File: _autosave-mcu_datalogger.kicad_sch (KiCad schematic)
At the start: 25 parts, among them U1 DS1337S_, U2 ATMEGA328P-AU, U3 24LC1025, U4 24LC1025, Y1 32.768MHz, Y2 16MHz

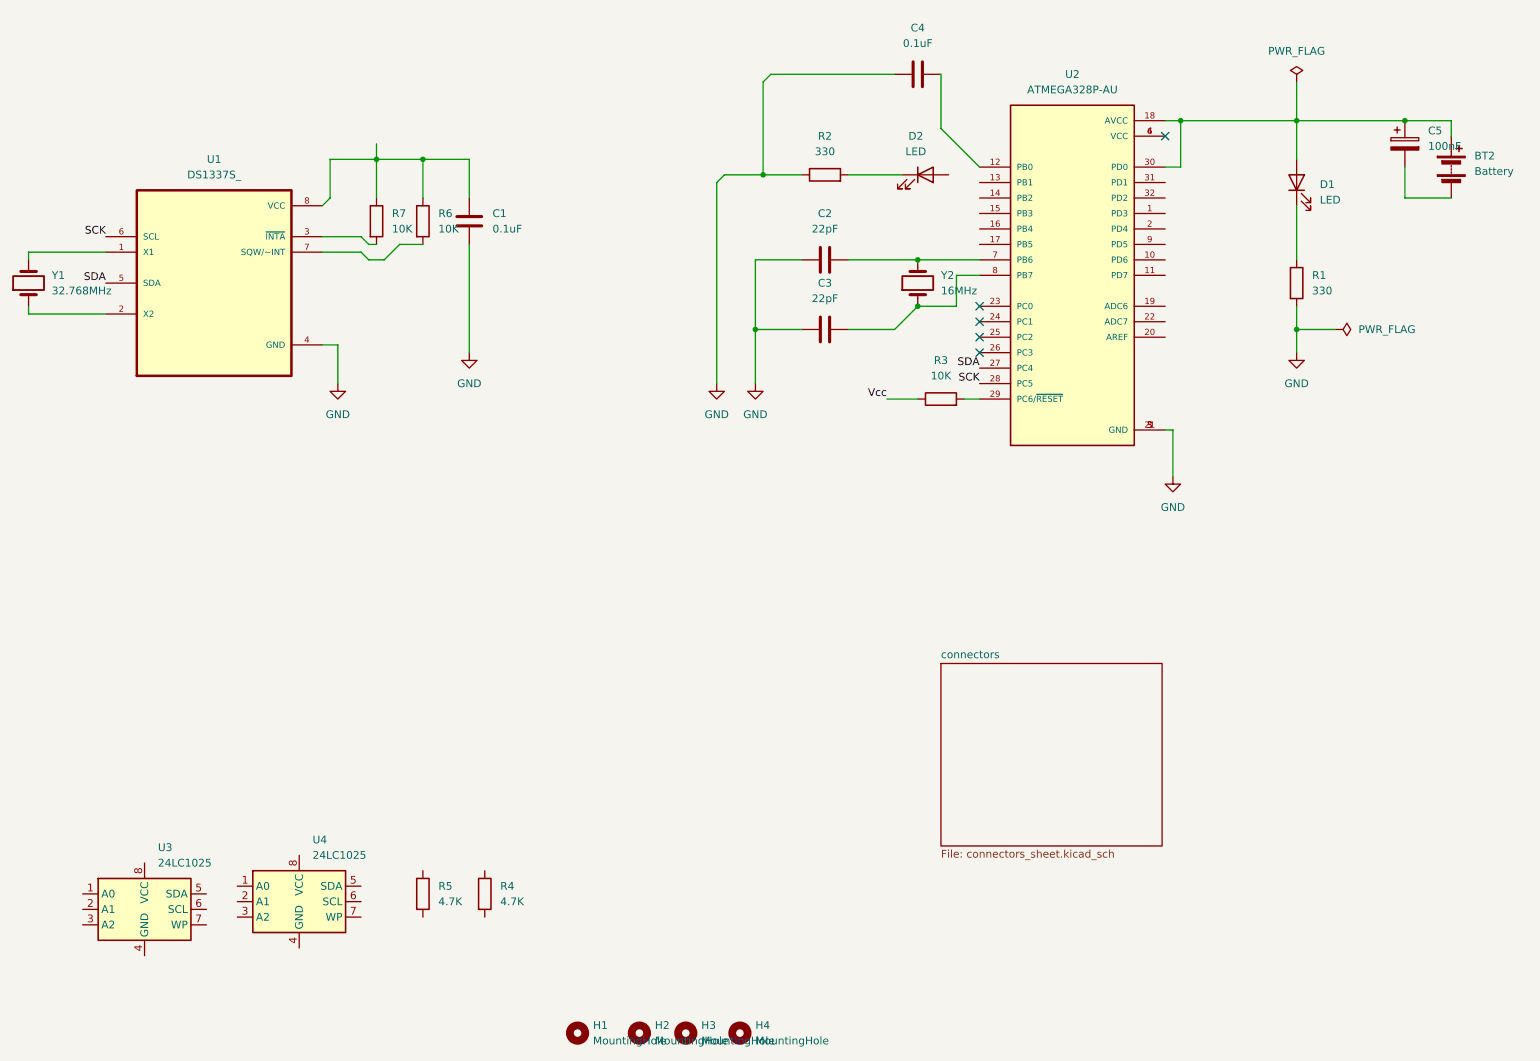
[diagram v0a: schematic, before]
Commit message: Complted the wiring of main sheet
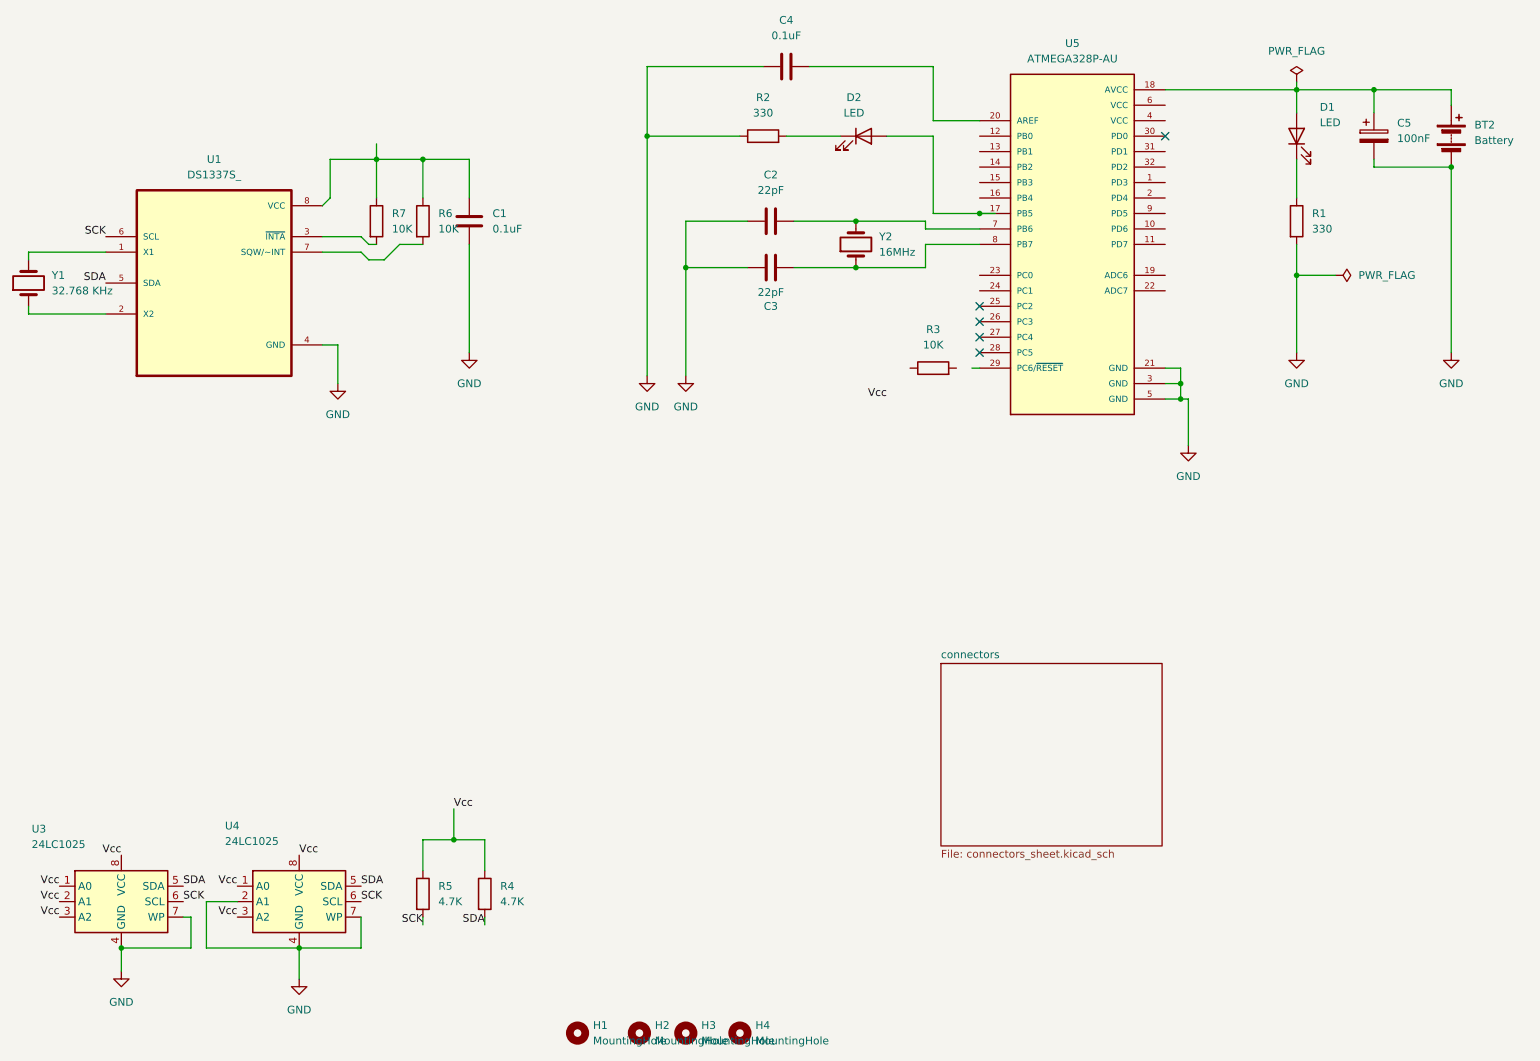
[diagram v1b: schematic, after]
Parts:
- removed U2: ATMEGA328P-AU, ATMEGA328P-AU:QFP80P900X900X120-32N, symbol ATMEGA328P-AU:ATMEGA328P-AU
- added U5: ATMEGA328P-AU, ATMEGA328P-AU:QFP80P900X900X120-32N, symbol ATMEGA328P-AU:ATMEGA328P-AU
- Y1: value 32.768MHz -> 32.768 KHz
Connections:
- net GND: now also BT2.2 (-), C5.2, U3.4 (GND), U3.7 (WP), U4.2 (A1), U4.4 (GND), U4.7 (WP), U5.21 (GND), U5.3 (GND), U5.5 (GND)
- net SCK: now also R5.2, U3.6 (SCL), U4.6 (SCL)
- net SDA: now also R4.2, U3.5 (SDA), U4.5 (SDA)
- net Vcc: now also R4.1, R5.1, U3.1 (A0), U3.2 (A1), U3.3 (A2), U3.8 (VCC), U4.1 (A0), U4.3 (A2), U4.8 (VCC); no longer R3.1
- net at BT2.1 (+), C5.1, D1.2 (A): now also U5.18 (AVCC)
- net at C4.2: now also U5.20 (AREF)
- net at C2.2, Y2.2: now also U5.7 (PB6)
- net at C3.2, Y2.1: now also U5.8 (PB7)
- net at D2.2 (A): now also U5.17 (PB5)
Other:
- moved on the sheet: BT2, C2, C3, C4, C5, D1, D2, R1, R2, R3, U3, Y2
